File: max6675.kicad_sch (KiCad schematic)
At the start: 14 parts, among them J3 Conn_01x02_Socket, U3 AP2127R-3.3, U5 MAX31855KASA

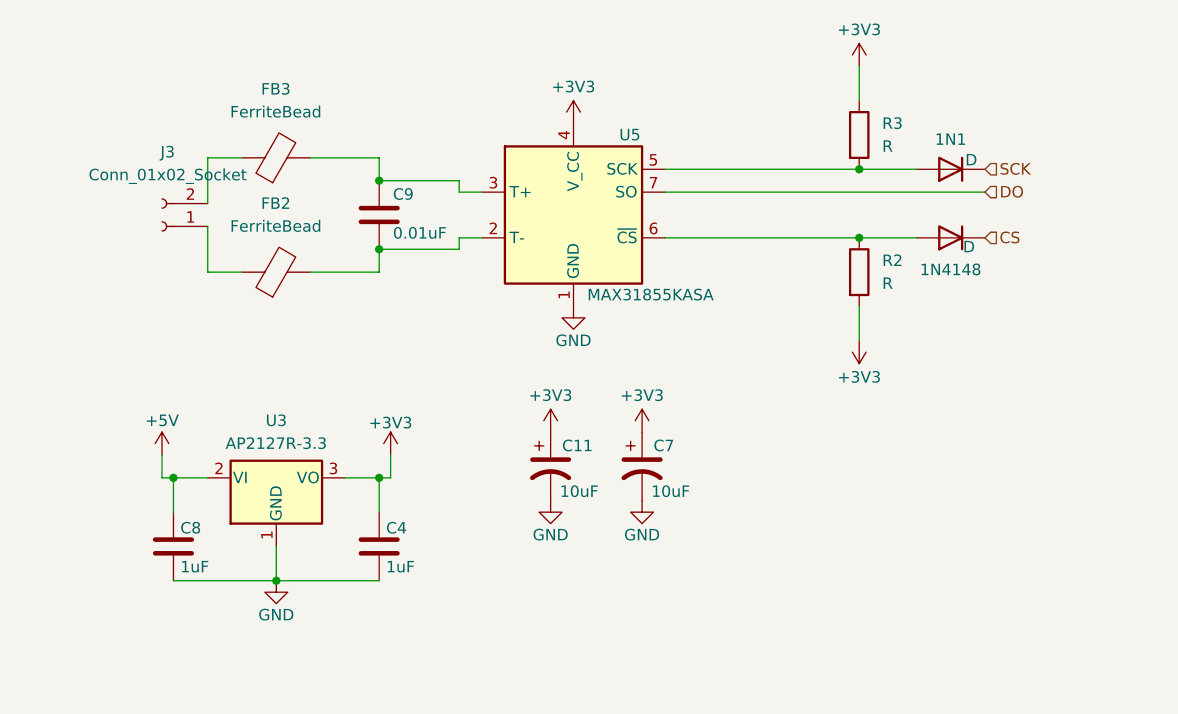
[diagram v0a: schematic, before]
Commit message: finalizes MAX boards & Begins PCB Design
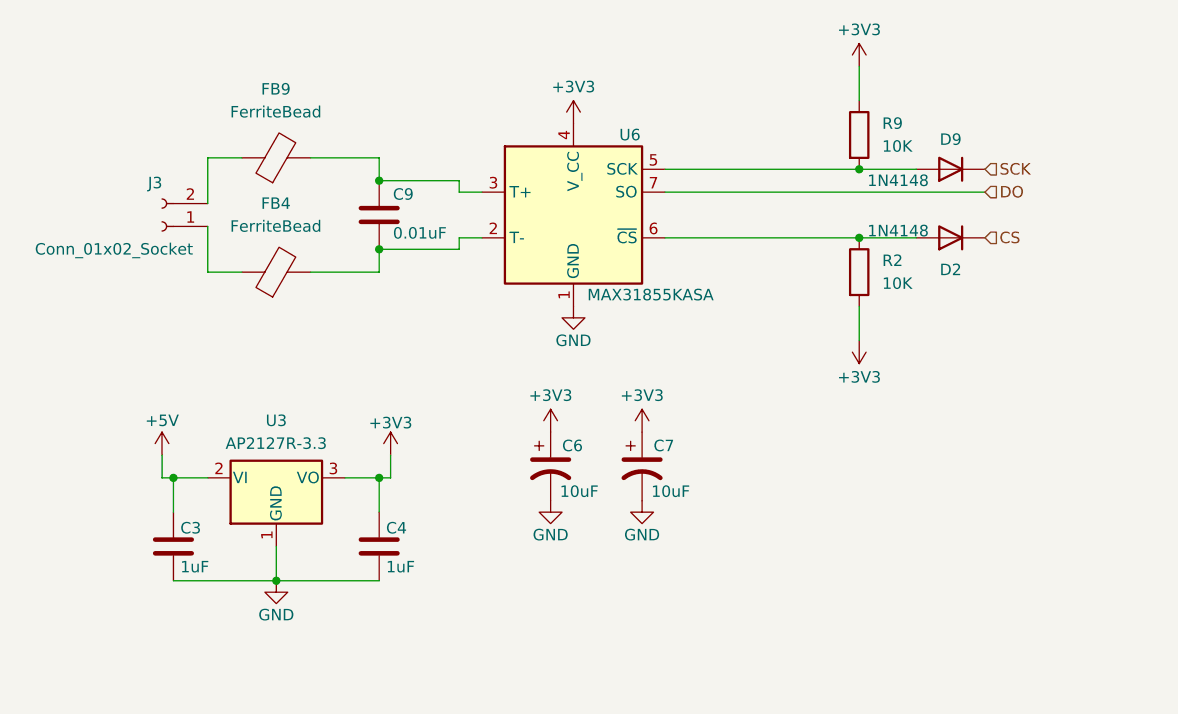
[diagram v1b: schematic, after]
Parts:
- removed FB2, FB3: FerriteBead, symbol Device:FerriteBead
- added FB4, FB9: FerriteBead, Inductor_SMD:L_0402_1005Metric, symbol Device:FerriteBead
- C6: renamed from C11; footprint (none) -> Capacitor_SMD:C_0504_1310Metric
- C7: footprint (none) -> Capacitor_SMD:C_0504_1310Metric
- C9: footprint (none) -> Capacitor_SMD:C_0402_1005Metric
- D2: renamed from 1N4148; value D -> 1N4148; footprint (none) -> Diode_SMD:D_1206_3216Metric
- D9: renamed from 1N1; value D -> 1N4148; footprint (none) -> Diode_SMD:D_1206_3216Metric
- R2: value R -> 10K
- R9: renamed from R3; value R -> 10K
- renumbered C8 to C3, U5 to U6
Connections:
- net at J3.2 (Pin_2): now also FB9.1
- net at C9.1, U6.3 (T+): now also FB9.2
- net at J3.1 (Pin_1): now also FB4.1
- net at C9.2, U6.2 (T-): now also FB4.2

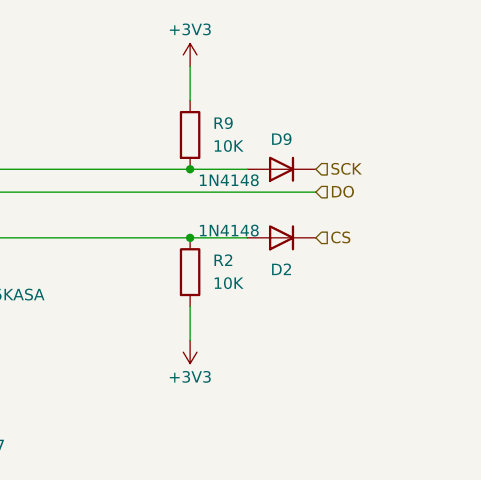
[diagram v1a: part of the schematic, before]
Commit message: PCB Wiring to ESP32
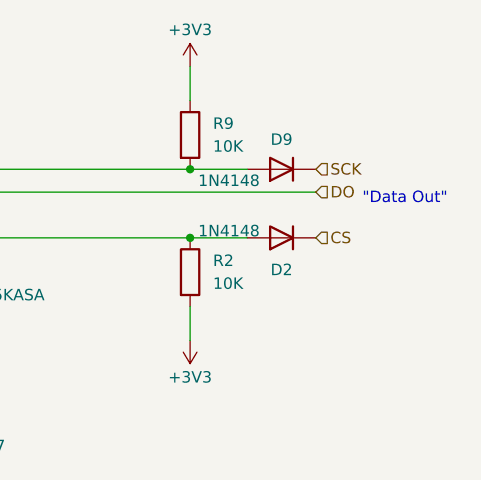
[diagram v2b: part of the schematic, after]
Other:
- note added: ""Data Out""
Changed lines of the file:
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@@
+		)
+	)
+	(text "\"Data Out\""
+		(exclude_from_sim no)
+		(at 130.556 43.942 0)
+		(effects
+			(font
+				(size 1.27 1.27)
+			)
 		)
 	)

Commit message: start compliance with PCBway
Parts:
- C3, C4: Item # (none) -> 3
- C6, C7: Item # (none) -> 4
- C9: Item # (none) -> 5
- D2, D9: Item # (none) -> 7
- FB4, FB9: Item # (none) -> 8
- J3: footprint TerminalBlock_4Ucon:TerminalBlock_4Ucon_1x02_P3.50mm_Horizontal -> TerminalBlock:TerminalBlock_bornier-2_P5.08mm; Item # (none) -> 10
- R2, R9: Item # (none) -> 16
- U3: Item # (none) -> 19
- U6: Item # (none) -> 21
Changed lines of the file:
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@@
+			)
+		)
+		(property "Item #" "16"
+			(at 106.68 52.07 0)
+			(effects
+				(font
+					(size 1.27 1.27)
+				)
+				(hide yes)
 			)
 		)
@@
 		)
 		(property "Description" "Polarized capacitor, US symbol"
+			(at 72.39 73.66 0)
+			(effects
+				(font
+					(size 1.27 1.27)
+				)
+				(hide yes)
+			)
+		)
+		(property "Item #" "4"
 			(at 72.39 73.66 0)
 			(effects
@@
 			)
 		)
+		(property "Item #" "19"
+			(at 41.91 74.93 0)
+			(effects
+				(font
+					(size 1.27 1.27)
+				)
+				(hide yes)
+			)
+		)
 		(pin "1"
 		)
@@
 		)
 		(property "Sim.Pins" "1=K 2=A"
+			(at 116.84 48.26 0)
+			(effects
+				(font
+					(size 1.27 1.27)
+				)
+				(hide yes)
+			)
+		)
+		(property "Item #" "7"
 			(at 116.84 48.26 0)
 			(effects
@@
 			)
 		)
+		(property "Item #" "8"
+			(at 41.91 52.07 0)
+			(effects
+				(font
+					(size 1.27 1.27)
+				)
+				(hide yes)
+			)
+		)
 		(pin "2"
 		)
@@
 			)
 		)
+		(property "Item #" "21"
+			(at 74.93 45.72 0)
+			(effects
+				(font
+					(size 1.27 1.27)
+				)
+				(hide yes)
+			)
+		)
 		(pin "7"
 		)
@@
 			)
 		)
+		(property "Item #" "3"
+			(at 30.48 82.55 0)
+			(effects
+				(font
+					(size 1.27 1.27)
+				)
+				(hide yes)
+			)
+		)
 		(pin "2"
 		)
@@
 			)
 		)
+		(property "Item #" "5"
+			(at 53.34 45.72 0)
+			(effects
+				(font
+					(size 1.27 1.27)
+				)
+				(hide yes)
+			)
+		)
 		(pin "1"
 		)
@@
 			)
 		)
+		(property "Item #" "3"
+			(at 53.34 82.55 0)
+			(effects
+				(font
+					(size 1.27 1.27)
+				)
+				(hide yes)
+			)
+		)
 		(pin "2"
 		)
@@
 			)
 		)
+		(property "Item #" "4"
+			(at 82.55 73.66 0)
+			(effects
+				(font
+					(size 1.27 1.27)
+				)
+				(hide yes)
+			)
+		)
 		(pin "2"
 		)
@@
 			)
 		)
-		(property "Footprint" "TerminalBlock_4Ucon:TerminalBlock_4Ucon_1x02_P3.50mm_Horizontal"
+		(property "Footprint" "TerminalBlock:TerminalBlock_bornier-2_P5.08mm"
 			(at 29.21 46.99 0)
 			(effects
@@
 		)
 		(property "Description" ""
+			(at 29.21 46.99 0)
+			(effects
+				(font
+					(size 1.27 1.27)
+				)
+				(hide yes)
+			)
+		)
+		(property "Item #" "10"
 			(at 29.21 46.99 0)
 			(effects
@@
 			)
 		)
+		(property "Item #" "16"
+			(at 106.68 36.83 0)
+			(effects
+				(font
+					(size 1.27 1.27)
+				)
+				(hide yes)
+			)
+		)
 		(pin "2"
 		)
@@
 			)
 		)
+		(property "Item #" "8"
+			(at 41.91 39.37 0)
+			(effects
+				(font
+					(size 1.27 1.27)
+				)
+				(hide yes)
+			)
+		)
 		(pin "2"
 		)
@@
 			(at 116.84 40.64 0)
 			(effects
+				(font
+					(size 1.27 1.27)
+				)
+				(hide yes)
+			)
+		)
+		(property "Item #" "7"
+			(at 116.84 40.64 0)
+			(effects

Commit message: edits to conform to design regulation
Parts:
- C3, C4, C9: footprint Capacitor_SMD:C_0402_1005Metric -> Capacitor_SMD:C_0201_0603Metric
- C6, C7: footprint Capacitor_SMD:C_0504_1310Metric -> Capacitor_SMD:C_0402_1005Metric
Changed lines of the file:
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@@
 			)
 		)
-		(property "Footprint" "Capacitor_SMD:C_0504_1310Metric"
+		(property "Footprint" "Capacitor_SMD:C_0402_1005Metric"
 			(at 72.39 73.66 0)
 			(effects
@@
 			)
 		)
-		(property "Footprint" "Capacitor_SMD:C_0402_1005Metric"
+		(property "Footprint" "Capacitor_SMD:C_0201_0603Metric"
 			(at 31.4452 86.36 0)
 			(effects
@@
 			)
 		)
-		(property "Footprint" "Capacitor_SMD:C_0402_1005Metric"
+		(property "Footprint" "Capacitor_SMD:C_0201_0603Metric"
 			(at 54.3052 49.53 0)
 			(effects
@@
 			)
 		)
-		(property "Footprint" "Capacitor_SMD:C_0402_1005Metric"
+		(property "Footprint" "Capacitor_SMD:C_0201_0603Metric"
 			(at 54.3052 86.36 0)
 			(effects
@@
 			)
 		)
-		(property "Footprint" "Capacitor_SMD:C_0504_1310Metric"
+		(property "Footprint" "Capacitor_SMD:C_0402_1005Metric"
 			(at 82.55 73.66 0)
 			(effects

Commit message: refresh stage 1
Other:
- moved on the sheet: C3, C4, C6, C7, U3

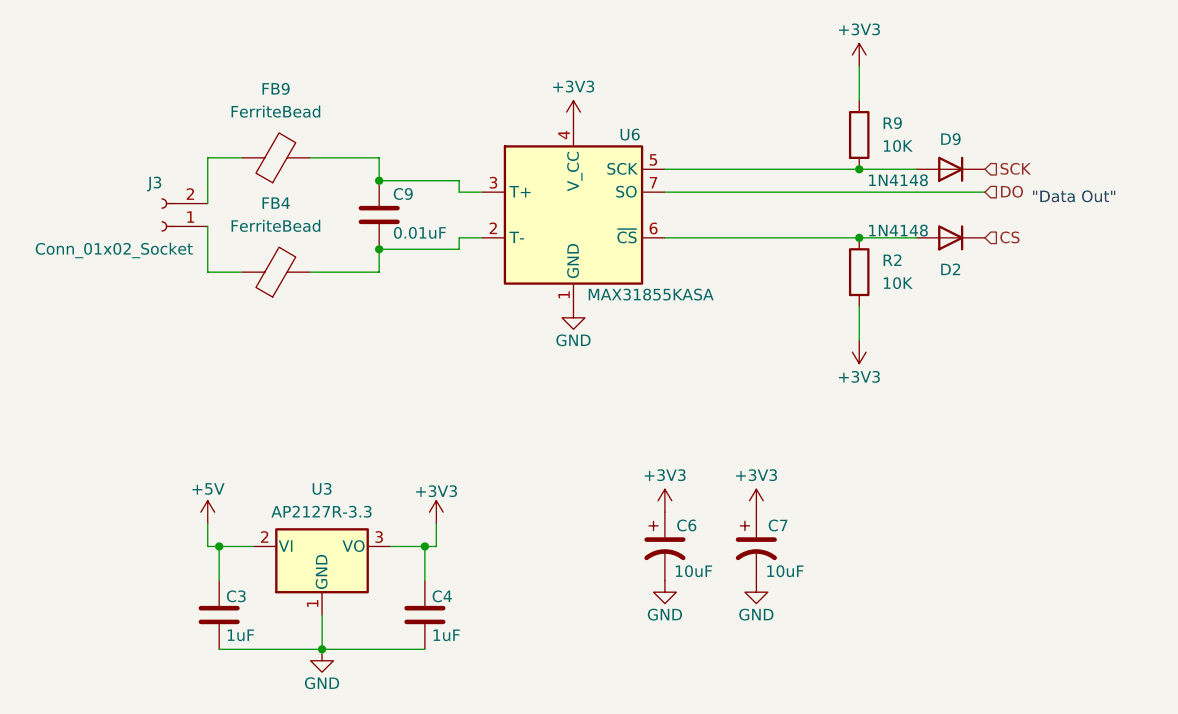
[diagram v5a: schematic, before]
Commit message: progress toward final board, need smaller relays
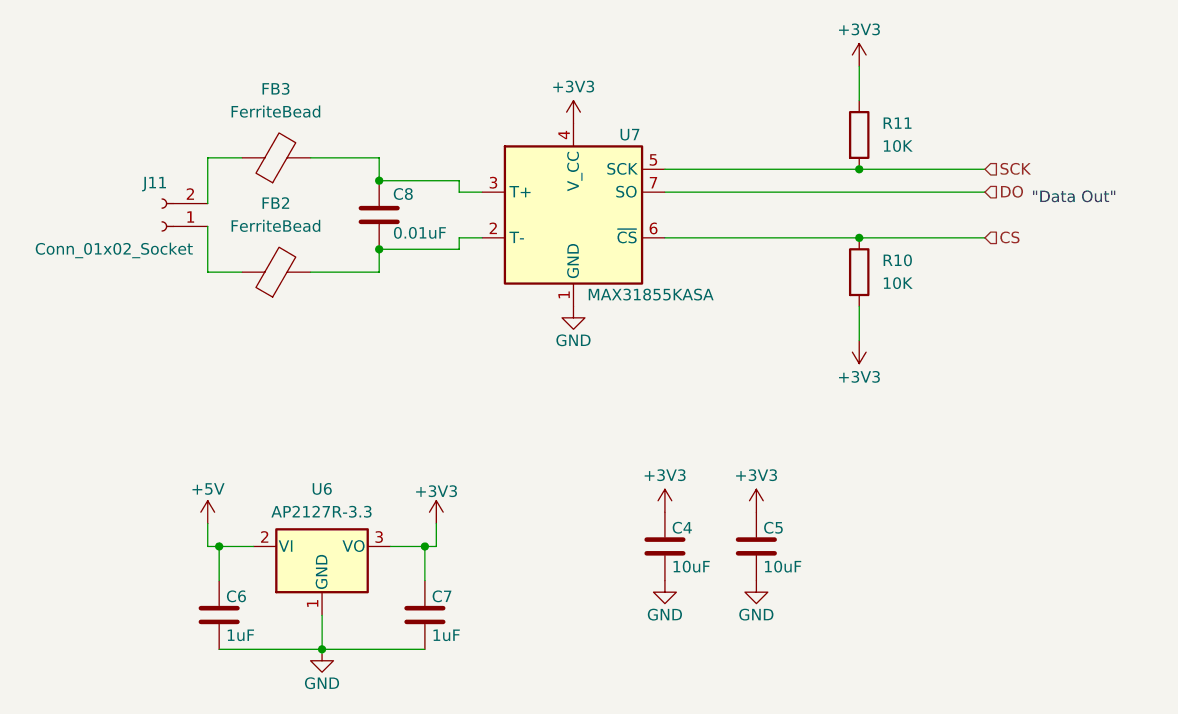
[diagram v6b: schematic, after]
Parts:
- removed C6, C7: 10uF, Capacitor_SMD:C_0402_1005Metric, symbol Device:C_Polarized_US
- removed D2, D9: 1N4148, Diode_SMD:D_1206_3216Metric, symbol Device:D
- added C4, C5: 10uF, Capacitor_SMD:C_0402_1005Metric, symbol Device:C
- C6: renamed from C3; footprint Capacitor_SMD:C_0201_0603Metric -> Capacitor_SMD:C_0402_1005Metric
- C7: renamed from C4; footprint Capacitor_SMD:C_0201_0603Metric -> Capacitor_SMD:C_0402_1005Metric
- C8: renamed from C9; footprint Capacitor_SMD:C_0201_0603Metric -> Capacitor_SMD:C_0402_1005Metric
- R10: renamed from R2; footprint Resistor_SMD:R_0402_1005Metric -> Resistor_SMD:R_0603_1608Metric
- R11: renamed from R9; footprint Resistor_SMD:R_0402_1005Metric -> Resistor_SMD:R_0603_1608Metric
- renumbered FB4 to FB2, FB9 to FB3, J3 to J11, U3 to U6, U6 to U7
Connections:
- net +3V3: now also C4.1, C5.1
- net CS: now also R10.1, U7.6 (~{CS})
- net GND: now also C4.2, C5.2
- net SCK: now also R11.2, U7.5 (SCK)

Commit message: begin new bom
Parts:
- removed C4, C5: 10uF, Capacitor_SMD:C_0402_1005Metric, symbol Device:C
- removed C6, C7: 1uF, Capacitor_SMD:C_0402_1005Metric, symbol Device:C
- removed U6: AP2127R-3.3, Package_TO_SOT_SMD:SOT-89-3, symbol Regulator_Linear:AP2127R-3.3
- added U12: MAX6675ISA+T, blastLib:SOIC-8_L5.0-W4.0-P1.27-LS6.0-BL, symbol blastLib:MAX6675ISA+T
- renumbered FB2 to FB4, J11 to J12, R10 to R12

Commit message: almost there
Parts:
- removed C8: 0.01uF, Capacitor_SMD:C_0402_1005Metric, symbol Device:C
- removed J12: Conn_01x02_Socket, TerminalBlock:TerminalBlock_bornier-2_P5.08mm, symbol Connector:Conn_01x02_Socket
- removed R11, R12: 10K, Resistor_SMD:R_0603_1608Metric, symbol Device:R
- removed U7: MAX31855KASA, Package_SO:SOIC-8_3.9x4.9mm_P1.27mm, symbol Sensor_Temperature:MAX31855KASA
- added C5: 100nF, Capacitor_SMD:C_0402_1005Metric, symbol Device:C
- added CN8: DB910-7.62-2P, blastLib:CONN-TH_2P-P7.62_DB910-7.62-2P, symbol blastLib:DB910-7.62-2P
- renumbered U12 to U8
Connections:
- net +3V3: now also U8.4 (VCC), C5.1
- net CS: now also U8.6 (~{CS})
- net DO: now also U8.7 (SO)
- net GND: now also FB3.2, U8.1 (GND), U8.2 (T-), C5.2
- net SCK: now also U8.5 (SCK)
- net at FB4.1: now also CN8.2
- net at FB4.2: now also U8.3 (T+)
- net at FB3.1: now also CN8.1
- no-connect marks 0 -> 1
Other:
- moved on the sheet: U8
